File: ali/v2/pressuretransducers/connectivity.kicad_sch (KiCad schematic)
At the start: 27 parts, among them J8 Conn_01x03, J9 Vertical Ethernet, U3 TJA1462ATK, U4 LAN8742AI, Y3 25 MHz

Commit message: Globally remove LCSC labels, update MPNs and IOCs, add +5V monitoring to DAQs, fix some footprints
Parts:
- C25: MPN GRM21A5C2J471FWA1 -> GRM1885C1H471JA01
- C27: MPN GRM21AR72A224KAC5 -> GRM188R71H224KAC4
- renumbered R8 to R10, R9 to R11, R10 to R12, R11 to R13, R12 to R14, R13 to R15, R14 to R16, R15 to R17, R16 to R18, R17 to R19, R18 to R20

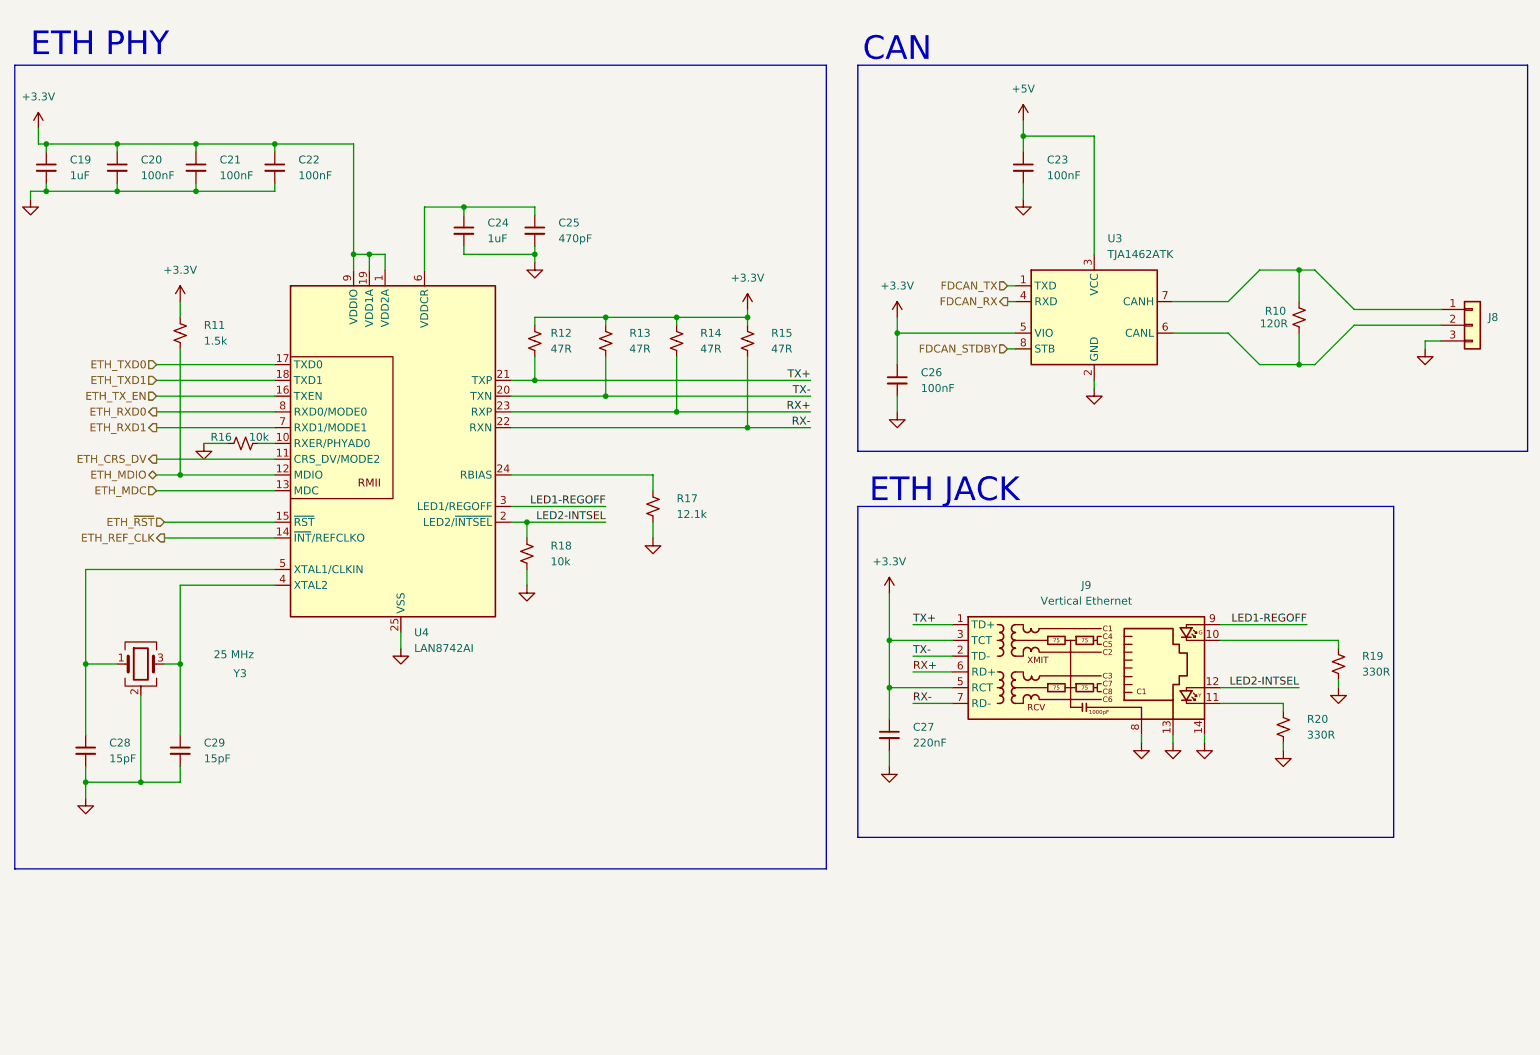
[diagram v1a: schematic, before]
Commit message: the great flatpak and kicad 10.0.6 migration
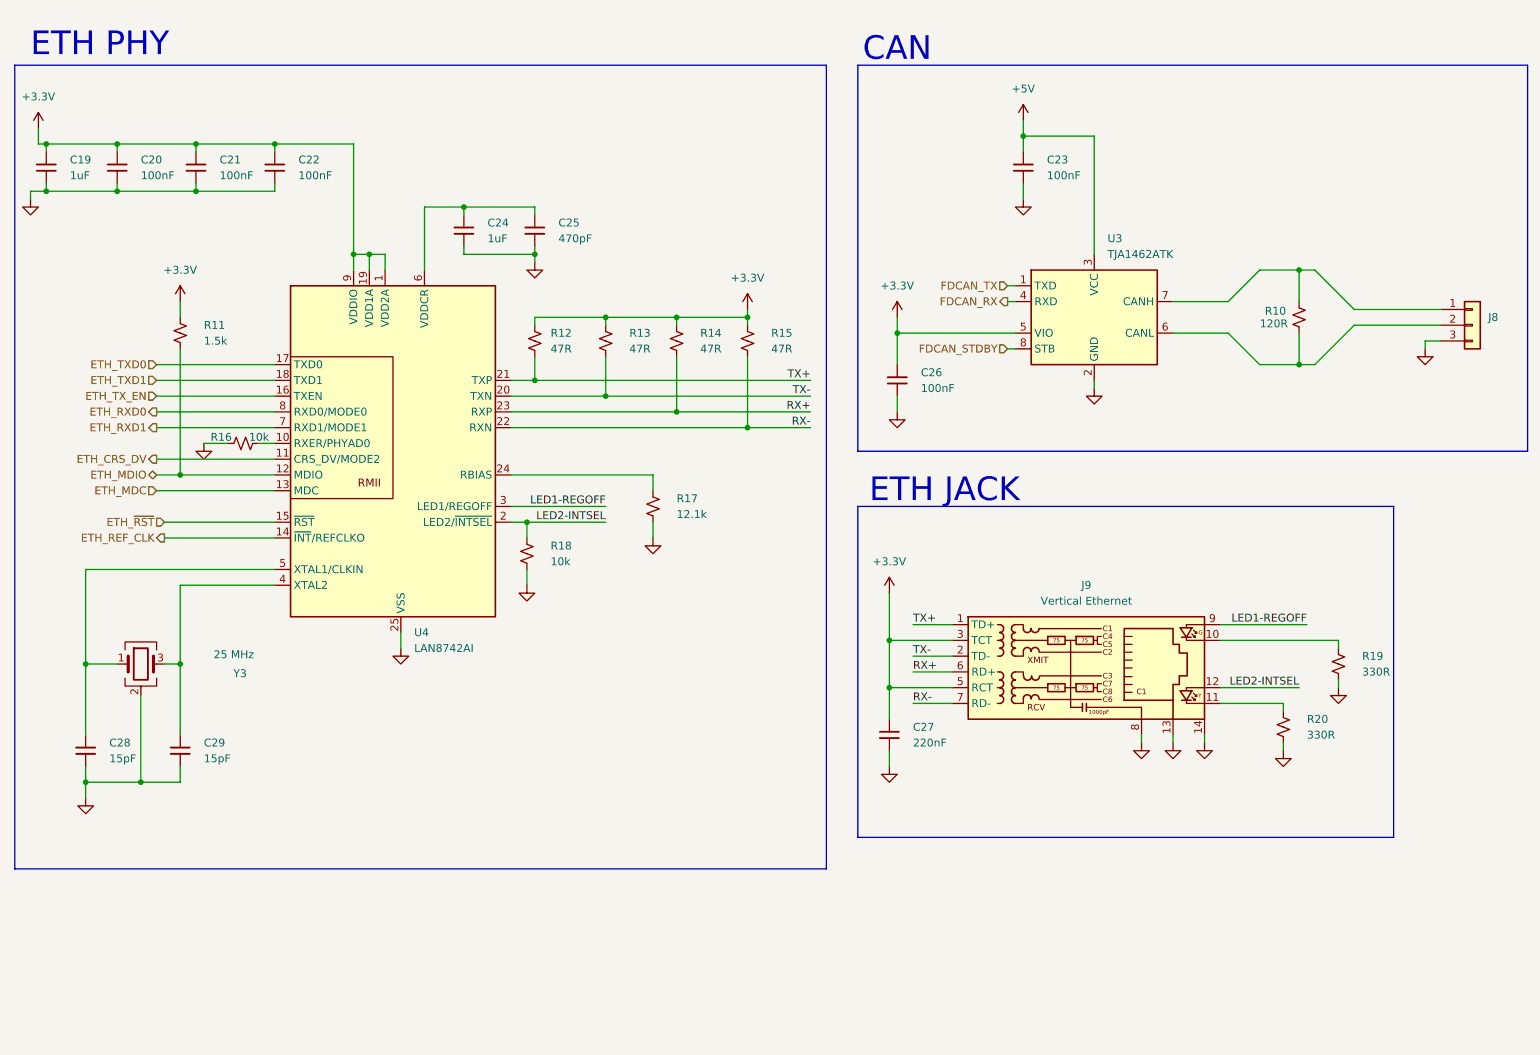
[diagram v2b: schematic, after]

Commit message: Commentary
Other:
- note added: "This sheet is pretty much unchanges from the original TC board"
- note added: "We agreed to just not populate this resistor if its not at the end as our layout will be fixed so it doesn't make sense to waste board space on adding jumpers"
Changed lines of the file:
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@@
 	(rectangle
 		(start 152.4 95.25)
-		(end 238.76 148.59)
+		(end 242.57 148.59)
 		(stroke
 			(width 0)
@@
 		)
 	)
+	(text "This sheet is pretty much unchanges from the original TC board"
+		(exclude_from_sim no)
+		(at 59.182 162.814 0)
+		(effects
+			(font
+				(size 1.27 1.27)
+			)
+		)
+	)
 	(text "CAN"
 		(exclude_from_sim no)
@@
 			)
 		)
+	)
+	(text "We agreed to just not populate this resistor if its not at the end\nas our layout will be fixed so it doesn't make sense to waste\nboard space on adding jumpers"
+		(exclude_from_sim no)
+		(at 218.948 82.55 0)
+		(effects
+			(font
+				(size 1.27 1.27)
+			)
+		)

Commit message: Fix 50R/60R widths
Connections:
- net CAN+: now reaches J8.1 (Pin_1), R10.2, U3.7 (CANH)
- net CAN-: now reaches J8.2 (Pin_2), R10.1, U3.6 (CANL)
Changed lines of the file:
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@@
+		)
+	)
+	(label "CAN-"
+		(at 205.7332 67.31 0)
+		(effects
+			(font
+				(size 1.27 1.27)
+			)
+			(justify left bottom)
+		)
+	)
+	(label "CAN+"
+		(at 205.74 62.23 0)
+		(effects
+			(font
+				(size 1.27 1.27)
+			)
+			(justify left bottom)
 		)
 	)

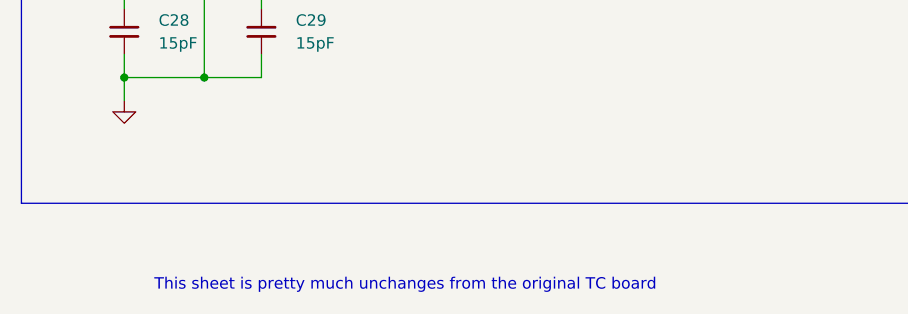
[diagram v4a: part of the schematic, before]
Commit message: Document setup, update template, and use an ampersand when referring to APRL
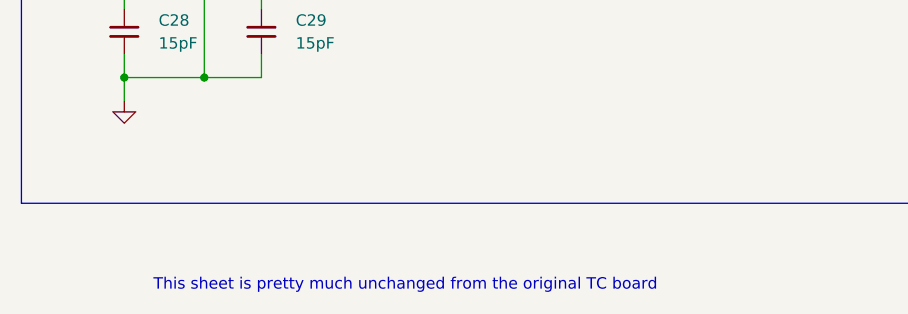
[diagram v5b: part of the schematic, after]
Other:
- note added: "This sheet is pretty much unchanged from the original TC board"
- note removed: "This sheet is pretty much unchanges from the original TC board"
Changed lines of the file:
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@@
 		)
 	)
-	(text "This sheet is pretty much unchanges from the original TC board"
+	(text "This sheet is pretty much unchanged from the original TC board"
 		(exclude_from_sim no)
 		(at 59.182 162.814 0)
@@
 		)
 	)
-	(label "CAN-"
-		(at 205.7332 67.31 0)
+	(label "TX+"
+		(at 144.78 74.93 180)
+		(effects
+			(font
+				(size 1.27 1.27)
+			)
+			(justify right bottom)
+		)
+	)
+	(label "LED2-INTSEL"
+		(at 223.52 124.46 180)
+		(effects
+			(font
+				(size 1.27 1.27)
+			)
+			(justify right bottom)
+		)
+	)
+	(label "LED2-INTSEL"
+		(at 111.76 97.79 180)
+		(effects
+			(font
+				(size 1.27 1.27)
+			)
+			(justify right bottom)
+		)
+	)
+	(label "TX-"
+		(at 161.29 119.38 0)
 		(effects
 			(font
@@
 		)
 	)
-	(label "TX+"
-		(at 144.78 74.93 180)
+	(label "CAN-"
+		(at 205.7332 67.31 0)
 		(effects
 			(font
-				(size 1.27 1.27)
-			)
-			(justify right bottom)
-		)
-	)
-	(label "LED2-INTSEL"
-		(at 223.52 124.46 180)
-		(effects
-			(font
-				(size 1.27 1.27)
-			)
-			(justify right bottom)
-		)
-	)
-	(label "LED2-INTSEL"
-		(at 111.76 97.79 180)
-		(effects
-			(font
-				(size 1.27 1.27)
-			)
-			(justify right bottom)
-		)
-	)
-	(label "TX-"
-		(at 161.29 119.38 0)
-		(effects
-			(font

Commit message: Begin prep for second board review
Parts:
- removed C29: 15pF, APRL_Passive:C_0603, symbol Device:C_Small
- removed J9: Vertical Ethernet, APRL_Connector:RJ45_Hanrun_HY951180A_Vertical, symbol APRL_Connector:RJ45_Hanrun_HY951180A
- removed R10: 120R, APRL_Passive:R_0603, symbol Device:R_Small_US
- removed R19, R20: 330R, APRL_Passive:R_0603, symbol Device:R_Small_US
- removed U3: TJA1462ATK, APRL_Package_QFN:HVSON-8-1EP_3x3mm_P0.65mm_EP1.6x2.4mm_ThermalVias, symbol APRL_Comms:TJA1462ATK
- removed U4: LAN8742AI, APRL_Package_QFN:VQFN-24-1EP_4x4mm_P0.5mm_EP2.5x2.5mm_ThermalVias, symbol APRL_Comms:LAN8742A
- removed Y3: 25 MHz, APRL_Passive:3225-4P-L, symbol Device:Crystal_GND24
- added C18: 1uF, APRL_Passive:C_0603, symbol Device:C_Small
- added J26: Vertical Ethernet, APRL_Connector:RJ45_Hanrun_HY951180A_Vertical, symbol APRL_Connector:RJ45_Hanrun_HY951180A
- added R51: 10k, APRL_Passive:R_0603, symbol Device:R_Small_US
- added R52, R53: 330R, APRL_Passive:R_0603, symbol Device:R_Small_US
- added U4: TJA1462ATK, APRL_Package_QFN:HVSON-8-1EP_3x3mm_P0.65mm_EP1.6x2.4mm_ThermalVias, symbol APRL_Comms:TJA1462ATK
- added U7: LAN8742AI, APRL_Package_QFN:VQFN-24-1EP_4x4mm_P0.5mm_EP2.5x2.5mm_ThermalVias, symbol APRL_Comms:LAN8742A
- added Y2: 25 MHz, APRL_Passive:3225-4P-L, symbol Device:Crystal_GND24
- C19: value 1uF -> 100nF; MPN GRM188D72A105KE01 -> GRM188R72A104KA35
- C23: value 100nF -> 1uF; MPN GRM188R72A104KA35 -> GRM188D72A105KE01
- C24: value 1uF -> 470pF; MPN GRM188D72A105KE01 -> GRM1885C1H471JA01
- C25: value 470pF -> 100nF; MPN GRM1885C1H471JA01 -> GRM188R72A104KA35
- C26: value 100nF -> 220nF; MPN GRM188R72A104KA35 -> GRM188R71H224KAC4
- C27: value 220nF -> 15pF; MPN GRM188R71H224KAC4 -> GRM1885C2E150FW07
- R11: value 1.5k -> 120R; MPN RC0603FR-071K5L -> AC0603FR-07120RL
- R12: value 47R -> 1.5k; MPN RC0603FR-0747RL -> RC0603FR-071K5L
- R16: value 10k -> 47R; MPN RC0603FR-0710KL -> RC0603FR-0747RL
- R17: value 12.1k -> 10k; MPN RT0603BRD0712K1L -> RC0603FR-0710KL
- R18: value 10k -> 12.1k; MPN RC0603FR-0710KL -> RT0603BRD0712K1L
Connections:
- net TX+ is gone; now on net ETH_MDIO: R12.2
- net +3.3V: now also C25.1, R16.1, C18.1, J26.3 (TCT), J26.5 (RCT), U4.5 (VIO), U7.1 (VDD2A), U7.19 (VDD1A), U7.9 (VDDIO); no longer C22.1, C27.1, R11.1
- net +5V: now also C22.1, U4.3 (VCC); no longer C23.1
- net ETH_CRS_DV: now also U7.11 (CRS_DV/MODE2)
- net ETH_MDC: now also U7.13 (MDC)
- net ETH_MDIO: now also U7.12 (MDIO); no longer R11.2
- net ETH_REF_CLK: now also U7.14 (~{INT}/REFCLKO)
- net ETH_RXD0: now also U7.8 (RXD0/MODE0)
- net ETH_RXD1: now also U7.7 (RXD1/MODE1)
- net ETH_TXD0: now also U7.17 (TXD0)
- net ETH_TXD1: now also U7.18 (TXD1)
- net ETH_TX_EN: now also U7.16 (TXEN)
- net ETH_~{RST}: now also U7.15 (~{RST})
- net FDCAN_RX: now also U4.4 (RXD)
- net FDCAN_STDBY: now also U4.8 (STB)
- net FDCAN_TX: now also U4.1 (TXD)
- net GND: now also R17.1, C18.2, J26.13, J26.14, J26.8, R51.2, R52.2, R53.2, U4.2 (GND), U4.9 (GND), U7.25 (VSS), Y2.2 (G), Y2.4 (G); no longer R16.1, R17.2
- net at C28.1: now also U7.4 (XTAL2), Y2.3
- net at C24.1: now also C23.1, U7.6 (VDDCR); no longer C25.1
- net at R16.2: now also J26.7 (RD-), U7.22 (RXN)
- net CAN+: no longer names the net of J8.1 (Pin_1)
- net CAN+: now also R11.2, U4.7 (CANH)
- net CAN-: no longer names the net of J8.2 (Pin_2)
- net CAN-: now also R11.1, U4.6 (CANL)
- net LED2-INTSEL: no longer names the net of R18.1
- net LED2-INTSEL: now also U7.24 (RBIAS)
- net RX+: no longer names the net of R14.2
- net RX+: now also J26.2 (TD-), U7.20 (TXN)
- net RX-: no longer names the net of R15.2
- net RX-: now also J26.6 (RD+), U7.23 (RXP)
- net TX-: no longer names the net of R13.2
- net TX-: now also J26.1 (TD+), U7.21 (TXP)
- new net: J26.11, R53.1
- new net: C27.1, U7.5 (XTAL1/CLKIN), Y2.1
- new net: J26.12, R51.1, U7.2 (LED2/~{INTSEL})
- new net: J26.10, R52.1
- new net: J26.9, U7.3 (LED1/REGOFF)
- new net: R17.2, U7.10 (RXER/PHYAD0)
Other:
- note added: "ETH"
- note removed: "ETH JACK"
- note removed: "ETH PHY"
- note removed: "This sheet is pretty much unchanged from the original TC board"
- note removed: "We agreed to just not populate this resistor if its not at the end as our layout will be fixed so it doesn't make sense to waste board space on adding jumpers"
